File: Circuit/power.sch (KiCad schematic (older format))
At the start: 19 parts, among them Q202 FDN340P, Q203 FDN340P, SW1 ON/OFF, U201 CN3063, U202 MCP6002, U3 LXDC2XQ

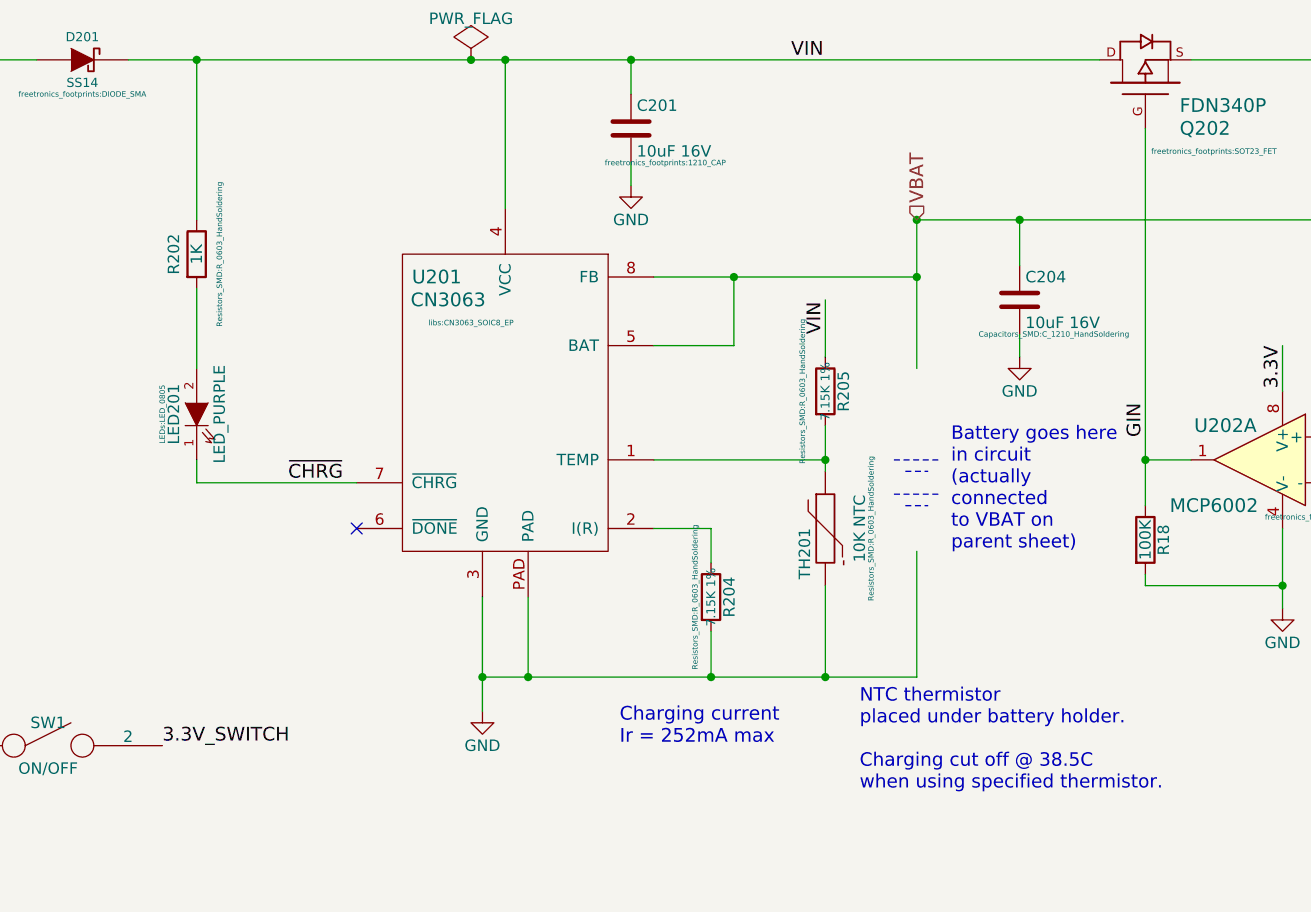
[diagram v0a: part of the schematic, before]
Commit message: Most power schematic component information added.
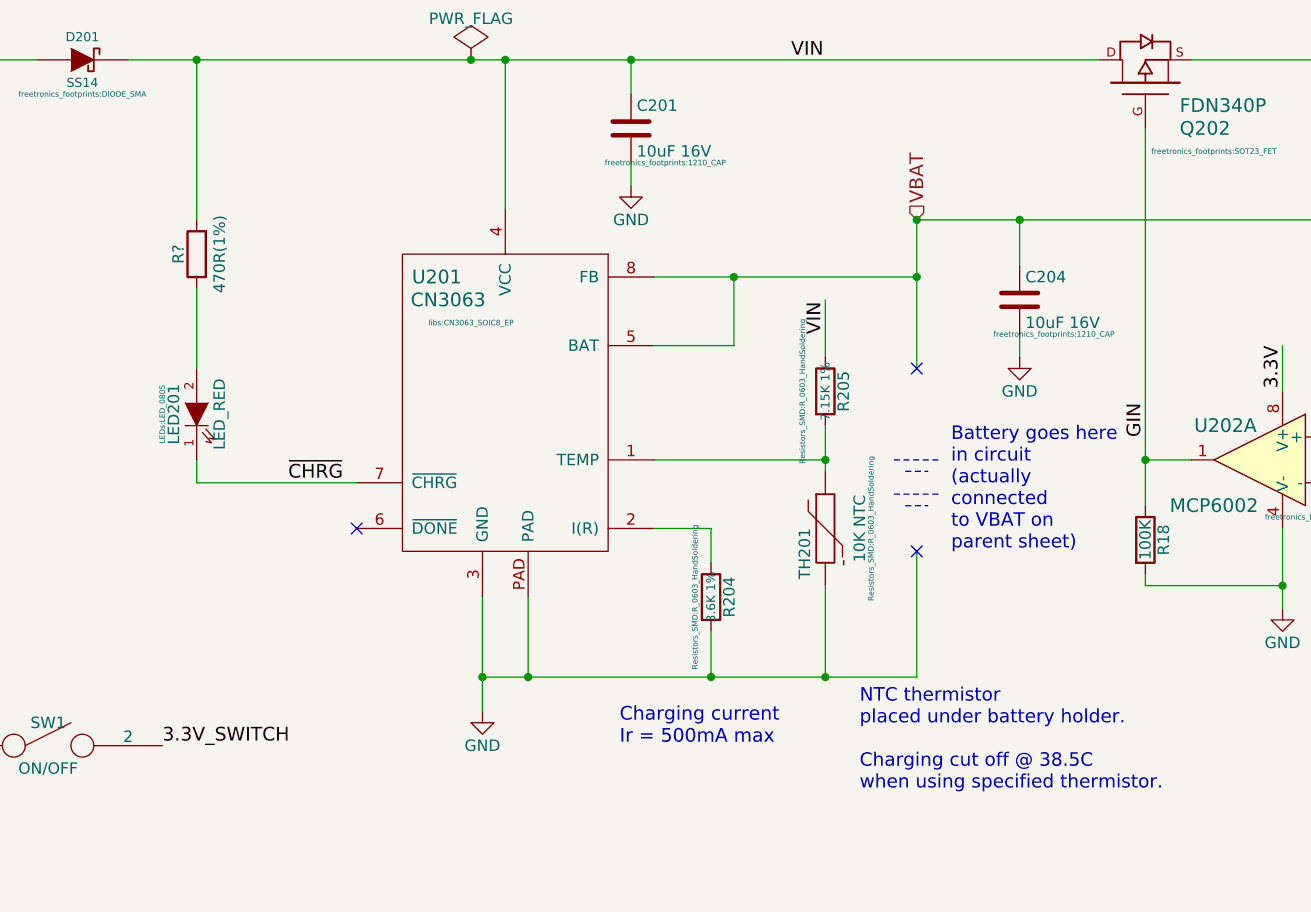
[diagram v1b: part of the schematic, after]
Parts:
- removed R202: 1K, Resistors_SMD:R_0603_HandSoldering, symbol R
- added R?: 470R(1%), Resistors_SMD:R_0603_HandSoldering, symbol R
- C201: Digikey PN (none) -> 1276-2865-1-ND; Link (none) -> http://www.digikey.com.au/product-detail/en/samsung-electro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; Manufacturer PN (none) -> CL32F106ZOHNNNE; Unit Cost (none) -> 0.29
- C204: footprint Capacitors_SMD:C_1210_HandSoldering -> freetronics_footprints:1210_CAP; Digikey PN (none) -> 1276-2865-1-ND; Link (none) -> http://www.digikey.com.au/product-detail/en/samsung-electro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; Manufacturer PN (none) -> CL32F106ZOHNNNE; Unit Cost (none) -> 0.29
- D201: Digikey PN (none) -> SS14CT-ND; Link (none) -> http://www.digikey.com.au/product-detail/en/fairchild-semic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; Manufacturer PN (none) -> SS14; Unit Cost (none) -> 0.39
- LED201: value LED_PURPLE -> LED_RED
- R204: value 7.15K 1% -> 3.6K 1%; Digikey PN (none) -> 311-3.60KHRCT-ND; Link (none) -> http://www.digikey.com.au/product-detail/en/yageo/RC0603FR-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; Manufacturer PN (none) -> RC0603FR-073K6L; Unit Cost (none) -> 0.10
- R205: Digikey PN (none) -> 311-7.15KHRCT-ND; Link (none) -> http://www.digikey.com.au/product-detail/en/yageo/RC0603FR-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; Manufacturer PN (none) -> RC0603FR-077K15L; Unit Cost (none) -> 0.10
- TH201: Digikey PN (none) -> 490-4800-1-ND; Link (none) -> http://www.digikey.com.au/product-detail/en/murata-electron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; MPN NCP18XH103F03RB -> (none); Manufacturer PN (none) -> NCP18XH103F03RB; Unit Cost (none) -> 0.23
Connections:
- no-connect marks 1 -> 3
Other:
- note added: "Charging current\nIr = 500mA max"
- note removed: "Charging current\nIr = 252mA max"
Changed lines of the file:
@@
 P 4950 4150
 F 0 "R204" V 5030 4150 50  0000 C CNN
-F 1 "7.15K 1%" V 4950 4150 39  0000 C CNN
+F 1 "3.6K 1%" V 4950 4150 39  0000 C CNN
 F 2 "Resistors_SMD:R_0603_HandSoldering" V 4880 4150 24  0000 C CNN
 F 3 "" H 4950 4150 30  0000 C CNN
+F 4 "311-3.60KHRCT-ND" V 4950 4150 60  0001 C CNN "Digikey PN"
+F 5 "http://www.digikey.com.au/product-detail/en/yageo/RC0603FR-073K6L/311-3.60KHRCT-ND/730079" V 4950 4150 60  0001 C CNN "Link"
+F 6 "RC0603FR-073K6L" V 4950 4150 60  0001 C CNN "Manufacturer PN"
+F 7 "0.10" V 4950 4150 60  0001 C CNN "Unit Cost"
 	1    4950 4150
 	1    0    0    -1
@@
 F 2 "freetronics_footprints:DIODE_SMA" H 2200 1650 24  0000 C CNN
 F 3 "" H 2200 1800 60  0000 C CNN
+F 4 "SS14CT-ND" H 2200 1800 60  0001 C CNN "Digikey PN"
+F 5 "http://www.digikey.com.au/product-detail/en/fairchild-semiconductor/SS14/SS14CT-ND/965729" H 2200 1800 60  0001 C CNN "Link"
+F 6 "SS14" H 2200 1800 60  0001 C CNN "Manufacturer PN"
+F 7 "0.39" H 2200 1800 60  0001 C CNN "Unit Cost"
 	1    2200 1800
 	1    0    0    -1
@@
 P 2700 3350
 F 0 "LED201" H 2700 3450 50  0000 C CNN
-F 1 "LED_PURPLE" H 2700 3250 50  0000 C CNN
+F 1 "LED_RED" H 2700 3250 50  0000 C CNN
 F 2 "LEDs:LED_0805" H 2700 3500 24  0000 C CNN
 F 3 "" H 2700 3350 60  0000 C CNN
 	1    2700 3350
 	0    -1   -1   0
-$EndComp
-$Comp
-L R R202
-U 1 1 563FF8B7
-P 2700 2650
-F 0 "R202" V 2600 2650 50  0000 C CNN
-F 1 "1K" V 2700 2650 50  0000 C CNN
-F 2 "Resistors_SMD:R_0603_HandSoldering" V 2800 2650 24  0000 C CNN
-F 3 "" H 2700 2650 60  0000 C CNN
-	1    2700 2650
-	1    0    0    -1
 $EndComp
 Text Label 3100 3650 0    60   ~ 0
@@
 USB Input:\nPreferred charging input if available, 4.5-5.5V
 Text Notes 4550 4800 0    60   ~ 0
-Charging current\nIr = 252mA max
+Charging current\nIr = 500mA max
 $Comp
 L GND #PWR032
@@
 F 2 "freetronics_footprints:1210_CAP" H 4750 1950 24  0000 C CNN
 F 3 "" H 4600 2100 60  0000 C CNN
+F 4 "1276-2865-1-ND" H 4600 2100 60  0001 C CNN "Digikey PN"
+F 5 "http://www.digikey.com.au/product-detail/en/samsung-electro-mechanics-america-inc/CL32F106ZOHNNNE/1276-2865-1-ND/3890951" H 4600 2100 60  0001 C CNN "Link"
+F 6 "CL32F106ZOHNNNE" H 4600 2100 60  0001 C CNN "Manufacturer PN"
+F 7 "0.29" H 4600 2100 60  0001 C CNN "Unit Cost"
 	1    4600 2100
 	1    0    0    -1
@@
 F 2 "Resistors_SMD:R_0603_HandSoldering" V 5350 3250 24  0000 C CNN
 F 3 "" H 5450 3250 60  0000 C CNN
+F 4 "311-7.15KHRCT-ND" V 5450 3250 60  0001 C CNN "Digikey PN"
+F 5 "http://www.digikey.com.au/product-detail/en/yageo/RC0603FR-077K15L/311-7.15KHRCT-ND/730310" V 5450 3250 60  0001 C CNN "Link"
+F 6 "RC0603FR-077K15L" V 5450 3250 60  0001 C CNN "Manufacturer PN"
+F 7 "0.10" V 5450 3250 60  0001 C CNN "Unit Cost"
 	1    5450 3250
 	1    0    0    -1
@@
 F 2 "Resistors_SMD:R_0603_HandSoldering" V 5650 3850 24  0000 C CNN
 F 3 "http://www.murata.com/products/catalog/pdf/r44e.pdf" H 5450 3850 60  0001 C CNN
-F 4 "NCP18XH103F03RB" V 5450 3850 60  0001 C CNN "MPN"
+F 4 "490-4800-1-ND" V 5450 3850 60  0001 C CNN "Digikey PN"
+F 5 "http://www.digikey.com.au/product-detail/en/murata-electronics-north-america/NCP18XH103F03RB/490-4800-1-ND/1644681" V 5450 3850 60  0001 C CNN "Link"
+F 6 "NCP18XH103F03RB" V 5450 3850 60  0001 C CNN "Manufacturer PN"
+F 7 "0.23" V 5450 3850 60  0001 C CNN "Unit Cost"
 	1    5450 3850
 	1    0    0    -1
@@
 Text Notes 5600 5000 0    59   ~ 0
 NTC thermistor\nplaced under battery holder.\n\nCharging cut off @ 38.5C\nwhen using specified thermistor.
-$Comp
-L C C204
-U 1 1 566F9EBD
-P 6300 2850
-F 0 "C204" H 6325 2950 50  0000 L CNN
-F 1 "10uF 16V" H 6325 2750 50  0000 L CNN
-F 2 "Capacitors_SMD:C_1210_HandSoldering" H 6450 2700 24  0000 C CNN
-F 3 "" H 6300 2850 60  0000 C CNN
-	1    6300 2850
-	1    0    0    -1
-$EndComp
 $Comp
 L GND #PWR039
@@
 	2700 3650 3400 3650
 NoConn ~ 3400 3850
+NoConn ~ 5850 3150
+NoConn ~ 5850 3950
+$Comp
+L R R?
+U 1 1 5820F348
+P 2700 2650
+F 0 "R?" V 2780 2650 50  0000 C CNN
+F 1 "470R(1%)" V 2600 2650 50  0000 C CNN
+F 2 "Resistors_SMD:R_0603_HandSoldering" V 2630 2650 50  0001 C CNN
+F 3 "" H 2700 2650 50  0000 C CNN
+F 4 "311-470HRCT-ND" V 2700 2650 60  0001 C CNN "Digikey PN"
+F 5 "http://www.digikey.com.au/product-detail/en/yageo/RC0603FR-07470RL/311-470HRCT-ND/730203" V 2700 2650 60  0001 C CNN "Link"
+F 6 "RC0603FR-07470RL" V 2700 2650 60  0001 C CNN "Manufacturer PN"
+F 7 "0.10" V 2700 2650 60  0001 C CNN "Unit Cost"
+	1    2700 2650
+	-1   0    0    1
+$EndComp
+$Comp
+L C C204
+U 1 1 5820F69B
+P 6300 2850
+F 0 "C204" H 6325 2950 50  0000 L CNN
+F 1 "10uF 16V" H 6325 2750 50  0000 L CNN
+F 2 "freetronics_footprints:1210_CAP" H 6450 2700 24  0000 C CNN
+F 3 "" H 6300 2850 60  0000 C CNN
+F 4 "1276-2865-1-ND" H 6300 2850 60  0001 C CNN "Digikey PN"
+F 5 "http://www.digikey.com.au/product-detail/en/samsung-electro-mechanics-america-inc/CL32F106ZOHNNNE/1276-2865-1-ND/3890951" H 6300 2850 60  0001 C CNN "Link"
+F 6 "CL32F106ZOHNNNE" H 6300 2850 60  0001 C CNN "Manufacturer PN"
+F 7 "0.29" H 6300 2850 60  0001 C CNN "Unit Cost"
+	1    6300 2850
+	1    0    0    -1
+$EndComp
 $EndSCHEMATC

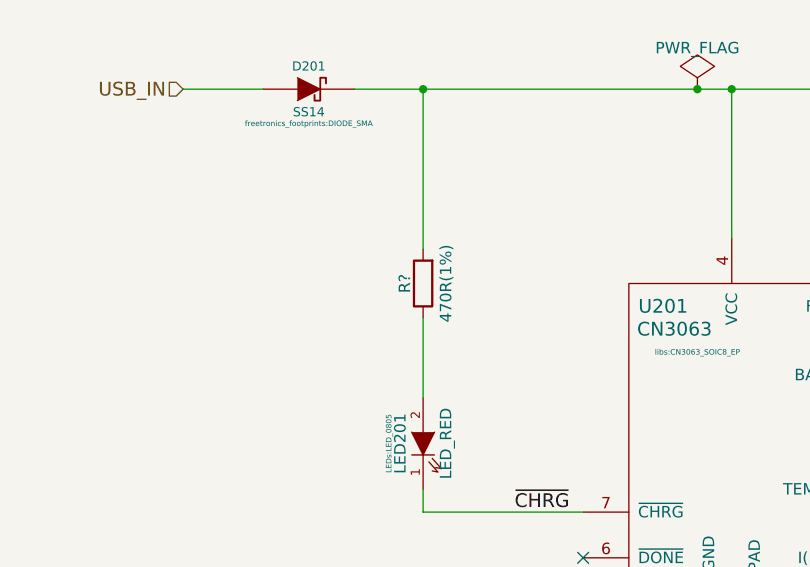
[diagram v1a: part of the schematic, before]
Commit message: Updated Alligator tabs
Incomplete.  Included to provide ideas.
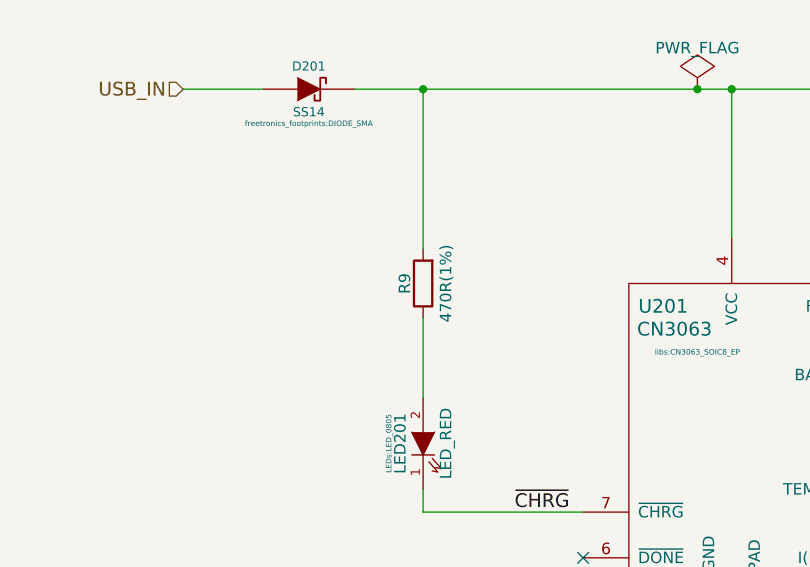
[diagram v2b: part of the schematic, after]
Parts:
- gave numbers to parts that had none: 1
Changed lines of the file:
@@
 NoConn ~ 5850 3950
 $Comp
-L R R?
+L R R9
 U 1 1 5820F348
 P 2700 2650
-F 0 "R?" V 2780 2650 50  0000 C CNN
+F 0 "R9" V 2780 2650 50  0000 C CNN
 F 1 "470R(1%)" V 2600 2650 50  0000 C CNN
 F 2 "Resistors_SMD:R_0603_HandSoldering" V 2630 2650 50  0001 C CNN
